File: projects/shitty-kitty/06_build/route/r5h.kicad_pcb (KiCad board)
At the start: 4 copper layers, 130 x 75 mm, 82 parts, among them J1 DC-005C-20A 12V, J2 TYPE-C-31-M-12, J3 ELECTRODES INNER, J4 ELECTRODES OUTER, J5 MOTOR NEMA17, J6 ENDSTOP TERM, J8 HOST 1x6, Q1 AOD4185 revpol, SW1 TS-1187A BOOT, SW2 TS-1187A RESET, U1 ESP32-S3-WROOM-1-N8R2, U2 TMC2209-LA-T, U3 MPR121QR2 0x5A, U4 MPR121QR2 0x5B, U5 MPR121QR2 0x5C, U6 MPR121QR2 0x5D, U7 LIS2DH12TR, U8 AP63205WU-7, U9 AMS1117-3.3

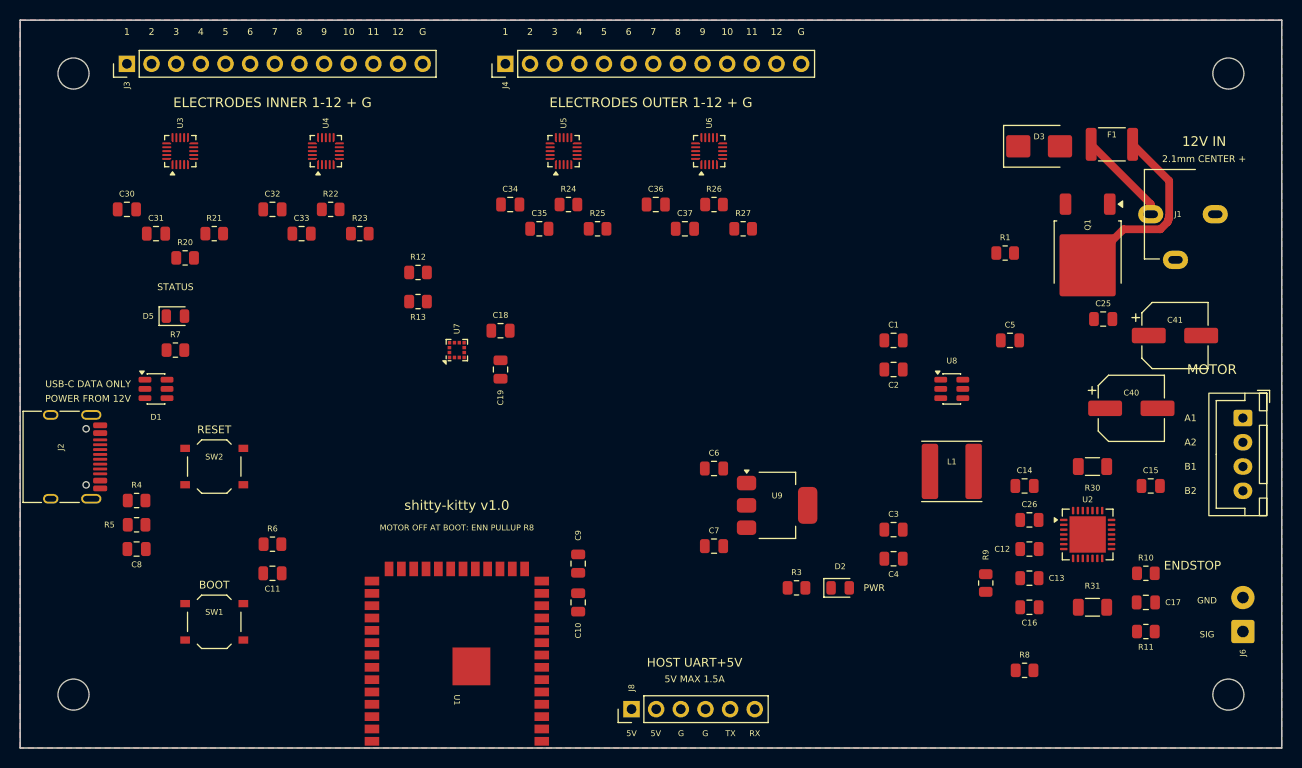
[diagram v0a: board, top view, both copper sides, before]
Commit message: shitty-kitty: WIP CHECKPOINT (not a gate) — routing surgery mid-flight, 18 DRC violations remain (6 clearance/5 hole_clr/6 h2h/1 conn_width from the SDA-via relocation), 0 unconnected. Route-surgery tooling: route_taps/route_unlock/lift_floors. Agent died on Fable credit wall; preserving work
Co-Authored-By: Claude Fable 5 <noreply@anthropic.com>
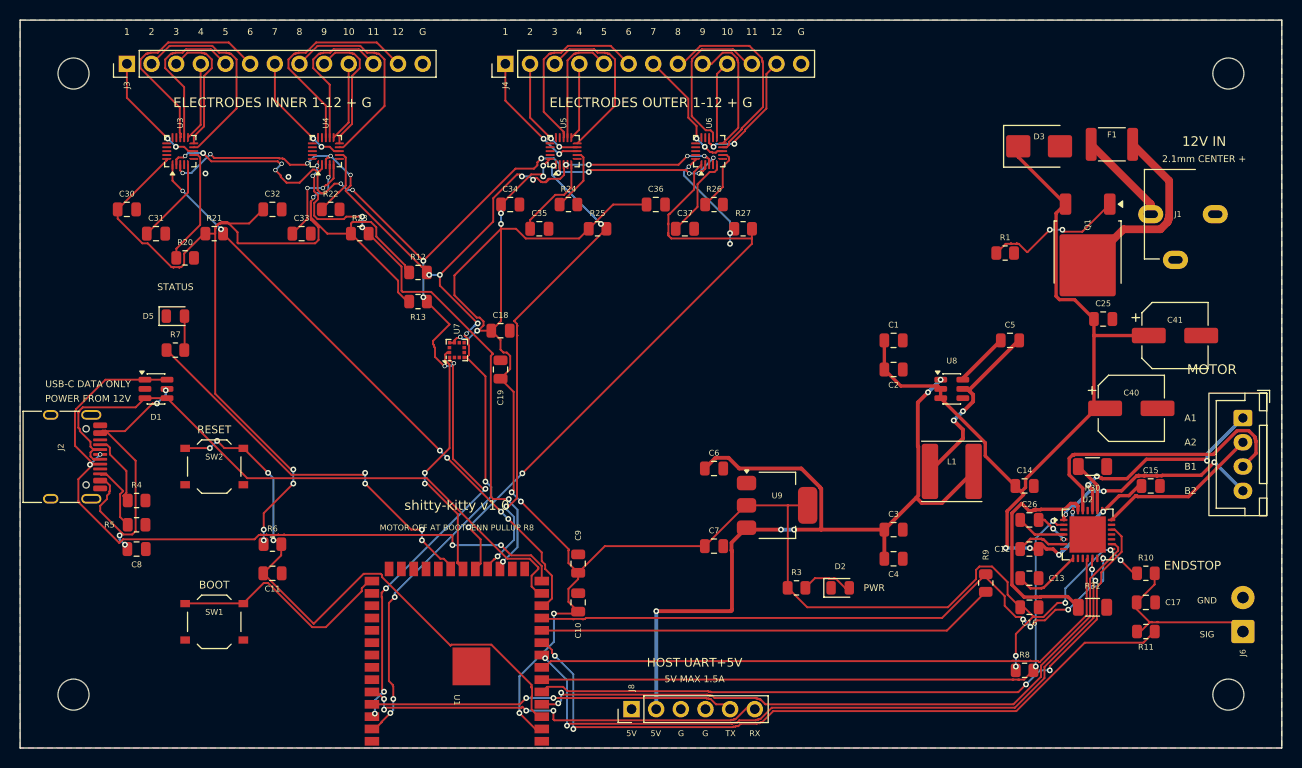
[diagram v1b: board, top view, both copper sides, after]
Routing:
- net 3V3: track 0.00 -> 324.3 mm, vias 0 -> 24
- net SCL: track 0.00 -> 134.0 mm, vias 0 -> 20
- net SDA: track 0.00 -> 130.2 mm, vias 0 -> 21
- net VIN_12V: track 0.00 -> 103.7 mm, vias 0 -> 5
- net 5V: track 0.00 -> 87.8 mm, vias 0 -> 5
- net USB_DP: track 0.00 -> 77.5 mm, vias 0 -> 4
- net ENDSTOP_G: track 0.00 -> 74.5 mm, vias 0 -> 2
- net INDEX: track 0.00 -> 74.3 mm, vias 0 -> 4
- net DIR: track 0.00 -> 71.9 mm, vias 0 -> 2
- net STEP: track 0.00 -> 71.4 mm, vias 0 -> 2
- net ENN: track 0.00 -> 68.6 mm, vias 0 -> 2
- net TMC_UART: track 0.00 -> 67.1 mm, vias 0 -> 4
- net USB_DM: track 0.00 -> 66.0 mm
- net MPR_IRQ4: track 0.00 -> 65.4 mm, vias 0 -> 2
- net DIAG: track 0.00 -> 64.5 mm
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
